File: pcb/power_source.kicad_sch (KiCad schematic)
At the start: 5 parts, among them J4 USB_C_Receptacle_USB2.0_14P

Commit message: pcb: satisfy ERC warnings and errors
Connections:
- net GND: no longer J4.A4 (VBUS), J4.A9 (VBUS), J4.B4 (VBUS), J4.B9 (VBUS), R36.1
- new net POWER_IN: J4.A4 (VBUS), J4.A9 (VBUS), J4.B4 (VBUS), J4.B9 (VBUS), R36.1
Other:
- note added: "red"
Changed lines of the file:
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@@
 	(generator_version "10.0")
 	(paper "A4")
-	(junction
-		(at 120.65 60.96)
-		(diameter 0)
-		(color 0 0 0 0)
-	)
-	(junction
-		(at 139.7 60.96)
-		(diameter 0)
-		(color 0 0 0 0)
-	)
-	(junction
-		(at 92.71 99.06)
-		(diameter 0)
-		(color 0 0 0 0)
-	)
-	(junction
-		(at 165.1 43.18)
-		(diameter 0)
-		(color 0 0 0 0)
-	)
-	(junction
-		(at 172.72 43.18)
-		(diameter 0)
-		(color 0 0 0 0)
-	)
-	(junction
-		(at 168.91 78.74)
-		(diameter 0)
-		(color 0 0 0 0)
-	)
-	(no_connect
-		(at 107.95 81.28)
-	)
-	(no_connect
-		(at 107.95 73.66)
-	)
-	(no_connect
-		(at 107.95 76.2)
-	)
-	(no_connect
-		(at 107.95 78.74)
-	)
-	(wire
-		(pts
-			(xy 85.09 99.06) (xy 92.71 99.06)
-		)
-		(stroke
-			(width 0)
-			(type default)
-		)
-	)
-	(wire
-		(pts
-			(xy 168.91 63.5) (xy 113.03 63.5)
-		)
-		(stroke
-			(width 0)
-			(type default)
-		)
-	)
-	(wire
-		(pts
-			(xy 165.1 43.18) (xy 180.34 43.18)
-		)
-		(stroke
-			(width 0)
-			(type default)
-		)
-	)
-	(wire
-		(pts
-			(xy 157.48 76.2) (xy 157.48 78.74)
-		)
-		(stroke
-			(width 0)
-			(type default)
-		)
-	)
-	(wire
-		(pts
-			(xy 113.03 63.5) (xy 113.03 66.04)
-		)
-		(stroke
-			(width 0)
-			(type default)
-		)
-	)
-	(wire
-		(pts
-			(xy 92.71 99.06) (xy 92.71 104.14)
-		)
-		(stroke
-			(width 0)
-			(type default)
-		)
-	)
-	(wire
-		(pts
-			(xy 120.65 99.06) (xy 120.65 60.96)
-		)
-		(stroke
-			(width 0)
-			(type default)
-		)
-	)
-	(wire
-		(pts
-			(xy 139.7 43.18) (xy 139.7 60.96)
-		)
-		(stroke
-			(width 0)
-			(type default)
-		)
-	)
-	(wire
-		(pts
-			(xy 168.91 76.2) (xy 168.91 78.74)
-		)
-		(stroke
-			(width 0)
-			(type default)
-		)
-	)
-	(wire
-		(pts
-			(xy 113.03 66.04) (xy 107.95 66.04)
-		)
-		(stroke
-			(width 0)
-			(type default)
-		)
-	)
-	(wire
-		(pts
-			(xy 92.71 99.06) (xy 120.65 99.06)
-		)
-		(stroke
-			(width 0)
-			(type default)
-		)
-	)
-	(wire
-		(pts
-			(xy 157.48 43.18) (xy 165.1 43.18)
-		)
-		(stroke
-			(width 0)
-			(type default)
-		)
-	)
-	(wire
-		(pts
-			(xy 149.86 43.18) (xy 139.7 43.18)
-		)
-		(stroke
-			(width 0)
-			(type default)
-		)
-	)
-	(wire
-		(pts
-			(xy 107.95 68.58) (xy 157.48 68.58)
-		)
-		(stroke
-			(width 0)
-			(type default)
-		)
-	)
-	(wire
-		(pts
-			(xy 107.95 60.96) (xy 120.65 60.96)
-		)
-		(stroke
-			(width 0)
-			(type default)
-		)
-	)
-	(wire
-		(pts
-			(xy 168.91 68.58) (xy 168.91 63.5)
-		)
-		(stroke
-			(width 0)
-			(type default)
-		)
-	)
-	(wire
-		(pts
-			(xy 180.34 46.99) (xy 180.34 43.18)
-		)
-		(stroke
-			(width 0)
-			(type default)
-		)
-	)
-	(wire
-		(pts
-			(xy 139.7 60.96) (xy 185.42 60.96)
-		)
-		(stroke
-			(width 0)
-			(type default)
-		)
-	)
-	(wire
-		(pts
-			(xy 168.91 78.74) (xy 168.91 80.01)
-		)
-		(stroke
-			(width 0)
-			(type default)
-		)
-	)
-	(wire
-		(pts
-			(xy 120.65 60.96) (xy 139.7 60.96)
-		)
-		(stroke
-			(width 0)
-			(type default)
-		)
-	)
-	(wire
-		(pts
-			(xy 157.48 78.74) (xy 168.91 78.74)
-		)
-		(stroke
-			(width 0)
-			(type default)
-		)
-	)
-	(label "red"
+	(text "red"
+		(exclude_from_sim no)
 		(at 175.26 43.18 0)
 		(effects
@@
 		)
 	)
+	(junction
+		(at 139.7 60.96)
+		(diameter 0)
+		(color 0 0 0 0)
+	)
+	(junction
+		(at 92.71 99.06)
+		(diameter 0)
+		(color 0 0 0 0)
+	)
+	(junction
+		(at 165.1 43.18)
+		(diameter 0)
+		(color 0 0 0 0)
+	)
+	(junction
+		(at 172.72 43.18)
+		(diameter 0)
+		(color 0 0 0 0)
+	)
+	(junction
+		(at 168.91 78.74)
+		(diameter 0)
+		(color 0 0 0 0)
+	)
+	(no_connect
+		(at 107.95 81.28)
+	)
+	(no_connect
+		(at 107.95 73.66)
+	)
+	(no_connect
+		(at 107.95 76.2)
+	)
+	(no_connect
+		(at 107.95 78.74)
+	)
+	(wire
+		(pts
+			(xy 85.09 99.06) (xy 92.71 99.06)
+		)
+		(stroke
+			(width 0)
+			(type default)
+		)
+	)
+	(wire
+		(pts
+			(xy 168.91 63.5) (xy 113.03 63.5)
+		)
+		(stroke
+			(width 0)
+			(type default)
+		)
+	)
+	(wire
+		(pts
+			(xy 165.1 43.18) (xy 180.34 43.18)
+		)
+		(stroke
+			(width 0)
+			(type default)
+		)
+	)
+	(wire
+		(pts
+			(xy 157.48 76.2) (xy 157.48 78.74)
+		)
+		(stroke
+			(width 0)
+			(type default)
+		)
+	)
+	(wire
+		(pts
+			(xy 113.03 63.5) (xy 113.03 66.04)
+		)
+		(stroke
+			(width 0)
+			(type default)
+		)
+	)
+	(wire
+		(pts
+			(xy 92.71 99.06) (xy 92.71 104.14)
+		)
+		(stroke
+			(width 0)
+			(type default)
+		)
+	)
+	(wire
+		(pts
+			(xy 139.7 43.18) (xy 139.7 60.96)
+		)
+		(stroke
+			(width 0)
+			(type default)
+		)
+	)
+	(wire
+		(pts
+			(xy 168.91 76.2) (xy 168.91 78.74)
+		)
+		(stroke
+			(width 0)
+			(type default)
+		)
+	)
+	(wire
+		(pts
+			(xy 113.03 66.04) (xy 107.95 66.04)
+		)
+		(stroke
+			(width 0)
+			(type default)
+		)
+	)
+	(wire
+		(pts
+			(xy 157.48 43.18) (xy 165.1 43.18)
+		)
+		(stroke
+			(width 0)
+			(type default)
+		)
+	)
+	(wire
+		(pts
+			(xy 149.86 43.18) (xy 139.7 43.18)
+		)
+		(stroke
+			(width 0)
+			(type default)
+		)
+	)
+	(wire
+		(pts
+			(xy 107.95 68.58) (xy 157.48 68.58)
+		)
+		(stroke
+			(width 0)
+			(type default)
+		)
+	)
+	(wire
+		(pts
+			(xy 107.95 60.96) (xy 139.7 60.96)
+		)
+		(stroke
+			(width 0)
+			(type default)
+		)
+	)
+	(wire
+		(pts
+			(xy 168.91 68.58) (xy 168.91 63.5)
+		)
+		(stroke
+			(width 0)
+			(type default)
+		)
+	)
+	(wire
+		(pts
+			(xy 180.34 46.99) (xy 180.34 43.18)
+		)
+		(stroke
+			(width 0)
+			(type default)
+		)
+	)
+	(wire
+		(pts
+			(xy 139.7 60.96) (xy 185.42 60.96)
+		)
+		(stroke
+			(width 0)
+			(type default)
+		)
+	)
+	(wire
+		(pts
+			(xy 168.91 78.74) (xy 168.91 80.01)
+		)
+		(stroke
+			(width 0)
+			(type default)
+		)
+	)
+	(wire
+		(pts
+			(xy 157.48 78.74) (xy 168.91 78.74)
+		)
+		(stroke
+			(width 0)
+			(type default)
+		)
+	)

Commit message: layout prep
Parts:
- removed J4: USB_C_Receptacle_USB2.0_14P, Package_DFN_QFN:WDFN-10-1EP_3x3mm_P0.5mm_EP1.8x2.5mm, symbol Connector:USB_C_Receptacle_USB2.0_14P
- added J5: USB4110-GF-A, USB4110_GF_A:USB4110-GF-A_GCT, symbol USB4110_GF_A:USB4110-GF-A
- D13: value VBUS -> red; footprint (none) -> LED_SMD:LED_0805_2012Metric_Pad1.15x1.40mm_HandSolder
- R36, R37, R38: footprint Resistor_THT:R_Array_SIP13 -> Resistor_SMD:R_0805_2012Metric_Pad1.20x1.40mm_HandSolder
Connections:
- net GND: now also J5.A1-B12 (GND), J5.A12-B1 (GND), J5.A8 (SBU1), J5.B8 (SBU2); no longer D13.2 (A), R36.2
- net POWER_IN: now also J5.A4-B9 (VBUS), J5.A9-B4 (VBUS)
- net at R38.1: now also J5.A5 (CC1)
- net at R37.1: now also J5.B5 (CC2)
- new net: D13.2 (A), R36.2
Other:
- note removed: "red"

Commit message: updates labels
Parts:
- renumbered D13 to D4, R36 to R52, R37 to R53, R38 to R54
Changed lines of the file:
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@@
 		(dnp no)
 		(fields_autoplaced yes)
-		(property "Reference" "#PWR073"
+		(property "Reference" "#PWR076"
 			(at 180.34 53.34 0)
 			(hide yes)
@@
 			(project "tdt4295"
 				(path "/603dd496-f9c4-4a31-9104-19eec41ebc98/00be9b76-425d-4c6c-9c1d-55091adef36b"
-					(reference "#PWR073")
+					(reference "#PWR076")
 					(unit 1)
 				)
@@
 		(dnp no)
 		(fields_autoplaced yes)
-		(property "Reference" "R36"
+		(property "Reference" "R52"
 			(at 153.67 36.83 90)
 			(show_name no)
@@
 			(project "tdt4295"
 				(path "/603dd496-f9c4-4a31-9104-19eec41ebc98/00be9b76-425d-4c6c-9c1d-55091adef36b"
-					(reference "R36")
+					(reference "R52")
 					(unit 1)
 				)
@@
 		(dnp no)
 		(fields_autoplaced yes)
-		(property "Reference" "R38"
+		(property "Reference" "R54"
 			(at 171.45 71.1199 0)
 			(show_name no)
@@
 			(project "tdt4295"
 				(path "/603dd496-f9c4-4a31-9104-19eec41ebc98/00be9b76-425d-4c6c-9c1d-55091adef36b"
-					(reference "R38")
+					(reference "R54")
 					(unit 1)
 				)
@@
 		(dnp no)
 		(fields_autoplaced yes)
-		(property "Reference" "R37"
+		(property "Reference" "R53"
 			(at 160.02 71.1199 0)
 			(show_name no)
@@
 			(project "tdt4295"
 				(path "/603dd496-f9c4-4a31-9104-19eec41ebc98/00be9b76-425d-4c6c-9c1d-55091adef36b"
-					(reference "R37")
+					(reference "R53")
 					(unit 1)
 				)
@@
 		(dnp no)
 		(fields_autoplaced yes)
-		(property "Reference" "#PWR072"
+		(property "Reference" "#PWR075"
 			(at 168.91 86.36 0)
 			(hide yes)
@@
 			(project "tdt4295"
 				(path "/603dd496-f9c4-4a31-9104-19eec41ebc98/00be9b76-425d-4c6c-9c1d-55091adef36b"
-					(reference "#PWR072")
+					(reference "#PWR075")
 					(unit 1)
 				)
@@
 		(dnp no)
 		(fields_autoplaced yes)
-		(property "Reference" "D13"
+		(property "Reference" "D4"
 			(at 170.4975 35.56 0)
 			(show_name no)
@@
 			(project "tdt4295"
 				(path "/603dd496-f9c4-4a31-9104-19eec41ebc98/00be9b76-425d-4c6c-9c1d-55091adef36b"
-					(reference "D13")
+					(reference "D4")
 					(unit 1)
 				)
@@
 		(dnp no)
 		(fields_autoplaced yes)
-		(property "Reference" "#PWR071"
+		(property "Reference" "#PWR074"
 			(at 92.71 110.49 0)
 			(hide yes)
@@
 			(project "tdt4295"
 				(path "/603dd496-f9c4-4a31-9104-19eec41ebc98/00be9b76-425d-4c6c-9c1d-55091adef36b"
-					(reference "#PWR071")
-					(unit 1)
-				)
+					(reference "#PWR074")
+					(unit 1)
+				)

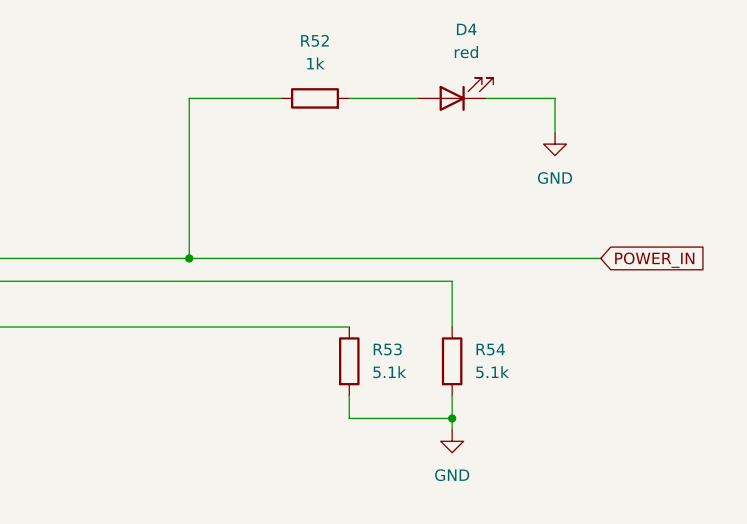
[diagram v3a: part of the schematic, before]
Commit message: pcb: address feedback
- make rgb565 resistor ladder
- add 1v0 diode
- clean up pwr flags
- remove unused mcu-sd spi
- use labels in mcu
- fix broken rgb diode
- connect usblc pin 5 to vbus
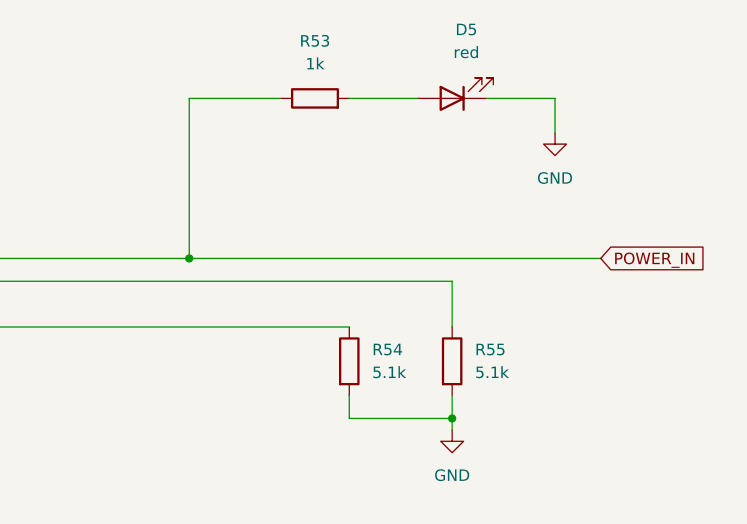
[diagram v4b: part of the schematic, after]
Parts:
- renumbered D4 to D5, R52 to R53, R53 to R54, R54 to R55
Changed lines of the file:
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@@
 		(dnp no)
 		(fields_autoplaced yes)
-		(property "Reference" "#PWR076"
+		(property "Reference" "#PWR078"
 			(at 180.34 53.34 0)
 			(hide yes)
@@
 			(project "tdt4295"
 				(path "/603dd496-f9c4-4a31-9104-19eec41ebc98/00be9b76-425d-4c6c-9c1d-55091adef36b"
-					(reference "#PWR076")
+					(reference "#PWR078")
 					(unit 1)
 				)
@@
 		(dnp no)
 		(fields_autoplaced yes)
-		(property "Reference" "R52"
+		(property "Reference" "R53"
 			(at 153.67 36.83 90)
 			(show_name no)
@@
 			(project "tdt4295"
 				(path "/603dd496-f9c4-4a31-9104-19eec41ebc98/00be9b76-425d-4c6c-9c1d-55091adef36b"
-					(reference "R52")
+					(reference "R53")
 					(unit 1)
 				)
@@
 		(dnp no)
 		(fields_autoplaced yes)
-		(property "Reference" "R54"
+		(property "Reference" "R55"
 			(at 171.45 71.1199 0)
 			(show_name no)
@@
 			(project "tdt4295"
 				(path "/603dd496-f9c4-4a31-9104-19eec41ebc98/00be9b76-425d-4c6c-9c1d-55091adef36b"
-					(reference "R54")
+					(reference "R55")
 					(unit 1)
 				)
@@
 		(dnp no)
 		(fields_autoplaced yes)
-		(property "Reference" "R53"
+		(property "Reference" "R54"
 			(at 160.02 71.1199 0)
 			(show_name no)
@@
 			(project "tdt4295"
 				(path "/603dd496-f9c4-4a31-9104-19eec41ebc98/00be9b76-425d-4c6c-9c1d-55091adef36b"
-					(reference "R53")
+					(reference "R54")
 					(unit 1)
 				)
@@
 		(dnp no)
 		(fields_autoplaced yes)
-		(property "Reference" "#PWR075"
+		(property "Reference" "#PWR077"
 			(at 168.91 86.36 0)
 			(hide yes)
@@
 			(project "tdt4295"
 				(path "/603dd496-f9c4-4a31-9104-19eec41ebc98/00be9b76-425d-4c6c-9c1d-55091adef36b"
-					(reference "#PWR075")
+					(reference "#PWR077")
 					(unit 1)
 				)
@@
 		(dnp no)
 		(fields_autoplaced yes)
-		(property "Reference" "D4"
+		(property "Reference" "D5"
 			(at 170.4975 35.56 0)
 			(show_name no)
@@
 			(project "tdt4295"
 				(path "/603dd496-f9c4-4a31-9104-19eec41ebc98/00be9b76-425d-4c6c-9c1d-55091adef36b"
-					(reference "D4")
+					(reference "D5")
 					(unit 1)
 				)
@@
 		(dnp no)
 		(fields_autoplaced yes)
-		(property "Reference" "#PWR074"
+		(property "Reference" "#PWR076"
 			(at 92.71 110.49 0)
 			(hide yes)
@@
 			(project "tdt4295"
 				(path "/603dd496-f9c4-4a31-9104-19eec41ebc98/00be9b76-425d-4c6c-9c1d-55091adef36b"
-					(reference "#PWR074")
-					(unit 1)
-				)
+					(reference "#PWR076")
+					(unit 1)
+				)

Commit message: pcb
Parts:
- J6: renamed from J5; footprint USB4110_GF_A:USB4110-GF-A_GCT -> USB4110-GF-A_GCT
- renumbered D5 to D8, R53 to R57, R54 to R58, R55 to R59
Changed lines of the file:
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@@
 		(dnp no)
 		(fields_autoplaced yes)
-		(property "Reference" "#PWR078"
+		(property "Reference" "#PWR071"
 			(at 180.34 53.34 0)
 			(hide yes)
@@
 			(project "tdt4295"
 				(path "/603dd496-f9c4-4a31-9104-19eec41ebc98/00be9b76-425d-4c6c-9c1d-55091adef36b"
-					(reference "#PWR078")
+					(reference "#PWR071")
 					(unit 1)
 				)
@@
 		(dnp no)
 		(fields_autoplaced yes)
-		(property "Reference" "R53"
+		(property "Reference" "R57"
 			(at 153.67 36.83 90)
 			(show_name no)
@@
 			(project "tdt4295"
 				(path "/603dd496-f9c4-4a31-9104-19eec41ebc98/00be9b76-425d-4c6c-9c1d-55091adef36b"
-					(reference "R53")
+					(reference "R57")
+					(unit 1)
+				)
+			)
+		)
+	)
+	(symbol
+		(lib_id "power:GND")
+		(at 92.71 104.14 0)
+		(unit 1)
+		(body_style 1)
+		(exclude_from_sim no)
+		(in_bom yes)
+		(on_board yes)
+		(in_pos_files yes)
+		(dnp no)
+		(fields_autoplaced yes)
+		(property "Reference" "#PWR069"
+			(at 92.71 110.49 0)
+			(hide yes)
+			(show_name no)
+			(do_not_autoplace no)
+			(effects
+				(font
+					(size 1.27 1.27)
+				)
+			)
+		)
+		(property "Value" "GND"
+			(at 92.71 109.22 0)
+			(show_name no)
+			(do_not_autoplace no)
+			(effects
+				(font
+					(size 1.27 1.27)
+				)
+			)
+		)
+		(property "Footprint" ""
+			(at 92.71 104.14 0)
+			(hide yes)
+			(show_name no)
+			(do_not_autoplace no)
+			(effects
+				(font
+					(size 1.27 1.27)
+				)
+			)
+		)
+		(property "Datasheet" ""
+			(at 92.71 104.14 0)
+			(hide yes)
+			(show_name no)
+			(do_not_autoplace no)
+			(effects
+				(font
+					(size 1.27 1.27)
+				)
+			)
+		)
+		(property "Description" "Power symbol creates a global label with name \"GND\" , ground"
+			(at 92.71 104.14 0)
+			(hide yes)
+			(show_name no)
+			(do_not_autoplace no)
+			(effects
+				(font
+					(size 1.27 1.27)
+				)
+			)
+		)
+		(pin "1"
+		)
+		(instances
+			(project "tdt4295"
+				(path "/603dd496-f9c4-4a31-9104-19eec41ebc98/00be9b76-425d-4c6c-9c1d-55091adef36b"
+					(reference "#PWR069")
 					(unit 1)
 				)
@@
 		(dnp no)
 		(fields_autoplaced yes)
-		(property "Reference" "R55"
+		(property "Reference" "R59"
 			(at 171.45 71.1199 0)
 			(show_name no)
@@
 			(project "tdt4295"
 				(path "/603dd496-f9c4-4a31-9104-19eec41ebc98/00be9b76-425d-4c6c-9c1d-55091adef36b"
-					(reference "R55")
+					(reference "R59")
 					(unit 1)
 				)
@@
 		(dnp no)
 		(fields_autoplaced yes)
-		(property "Reference" "R54"
+		(property "Reference" "R58"
 			(at 160.02 71.1199 0)
 			(show_name no)
@@
 			(project "tdt4295"
 				(path "/603dd496-f9c4-4a31-9104-19eec41ebc98/00be9b76-425d-4c6c-9c1d-55091adef36b"
-					(reference "R54")
+					(reference "R58")
 					(unit 1)
 				)
@@
 		(dnp no)
 		(fields_autoplaced yes)
-		(property "Reference" "#PWR077"
+		(property "Reference" "#PWR070"
 			(at 168.91 86.36 0)
 			(hide yes)
@@
 			(project "tdt4295"
 				(path "/603dd496-f9c4-4a31-9104-19eec41ebc98/00be9b76-425d-4c6c-9c1d-55091adef36b"
-					(reference "#PWR077")
+					(reference "#PWR070")
 					(unit 1)
 				)
@@
 		(in_pos_files yes)
 		(dnp no)
-		(property "Reference" "J5"
+		(property "Reference" "J6"
 			(at 81.28 50.8 0)
 			(show_name no)
@@
 			)
 		)
-		(property "Footprint" "USB4110_GF_A:USB4110-GF-A_GCT"
+		(property "Footprint" "USB4110-GF-A_GCT"
 			(at 60.96 73.66 0)
 			(hide yes)
@@
 			(project "tdt4295"
 				(path "/603dd496-f9c4-4a31-9104-19eec41ebc98/00be9b76-425d-4c6c-9c1d-55091adef36b"
-					(reference "J5")
+					(reference "J6")
 					(unit 1)
 				)
@@
 		(dnp no)
 		(fields_autoplaced yes)
-		(property "Reference" "D5"
+		(property "Reference" "D8"
 			(at 170.4975 35.56 0)
 			(show_name no)
@@
 			(project "tdt4295"
 				(path "/603dd496-f9c4-4a31-9104-19eec41ebc98/00be9b76-425d-4c6c-9c1d-55091adef36b"
-					(reference "D5")
-					(unit 1)
-				)
-			)
-		)
-	)
-	(symbol
-		(lib_id "power:GND")
-		(at 92.71 104.14 0)
-		(unit 1)
-		(body_style 1)
-		(exclude_from_sim no)
-		(in_bom yes)
-		(on_board yes)
-		(in_pos_files yes)
-		(dnp no)
-		(fields_autoplaced yes)
-		(property "Reference" "#PWR076"
-			(at 92.71 110.49 0)
-			(hide yes)
-			(show_name no)
-			(do_not_autoplace no)
-			(effects
-				(font
-					(size 1.27 1.27)
-				)
-			)
-		)
-		(property "Value" "GND"
-			(at 92.71 109.22 0)
-			(show_name no)
-			(do_not_autoplace no)
-			(effects
-				(font
-					(size 1.27 1.27)
-				)
-			)
-		)
-		(property "Footprint" "QFN12_TCPP01-M12_STM"
-			(at 92.71 104.14 0)
-			(hide yes)
-			(show_name no)
-			(do_not_autoplace no)
-			(effects
-				(font
-					(size 1.27 1.27)
-				)
-			)
-		)
-		(property "Datasheet" ""
-			(at 92.71 104.14 0)
-			(hide yes)
-			(show_name no)
-			(do_not_autoplace no)
-			(effects
-				(font
-					(size 1.27 1.27)
-				)
-			)
-		)
-		(property "Description" "Power symbol creates a global label with name \"GND\" , ground"
-			(at 92.71 104.14 0)
-			(hide yes)
-			(show_name no)
-			(do_not_autoplace no)
-			(effects
-				(font
-					(size 1.27 1.27)
-				)
-			)
-		)
-		(pin "1"
-		)
-		(instances
-			(project "tdt4295"
-				(path "/603dd496-f9c4-4a31-9104-19eec41ebc98/00be9b76-425d-4c6c-9c1d-55091adef36b"
-					(reference "#PWR076")
-					(unit 1)
-				)
+					(reference "D8")
+					(unit 1)
+				)
